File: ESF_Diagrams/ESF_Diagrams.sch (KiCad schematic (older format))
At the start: 37 parts, among them M1 Motor, M2 Motor, U2 AIR, U3 AIR

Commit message: Fix 2
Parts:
- added BT? (x48): Battery_Cell, symbol Battery_Cell
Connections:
- wire segments 88 -> 123
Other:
- moved on the sheet: BT?

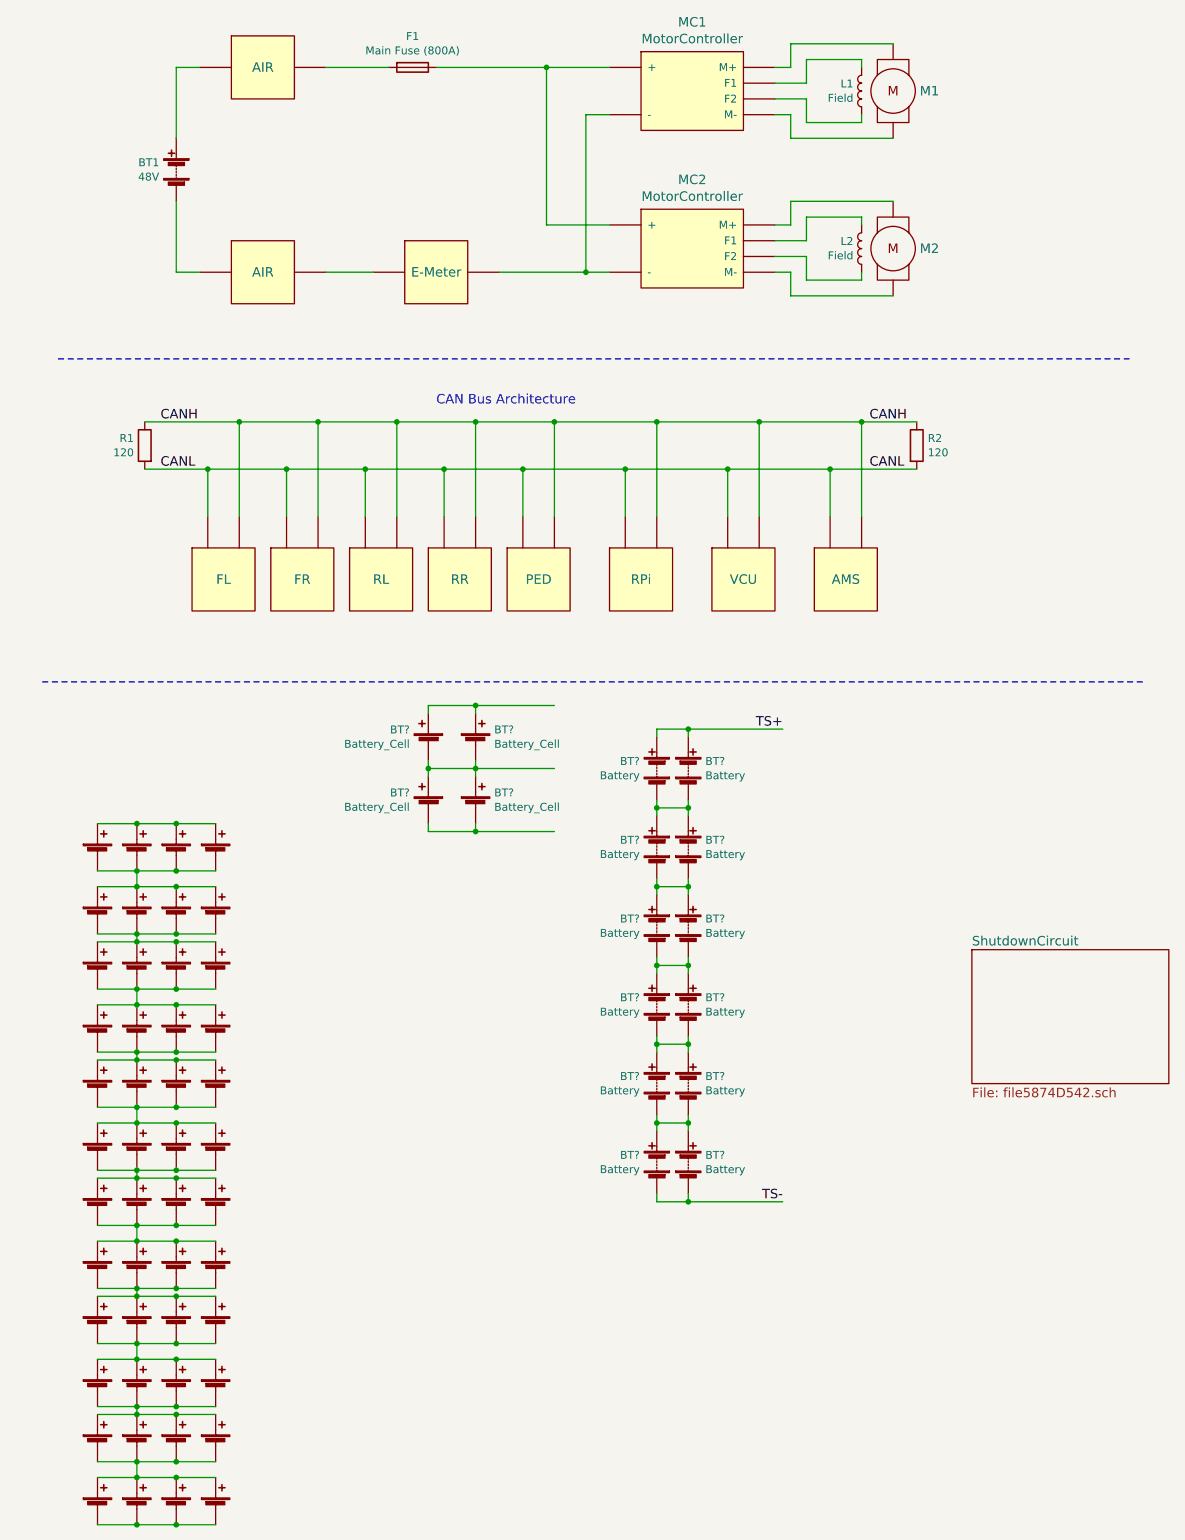
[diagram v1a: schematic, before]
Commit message: Remake battery drawing
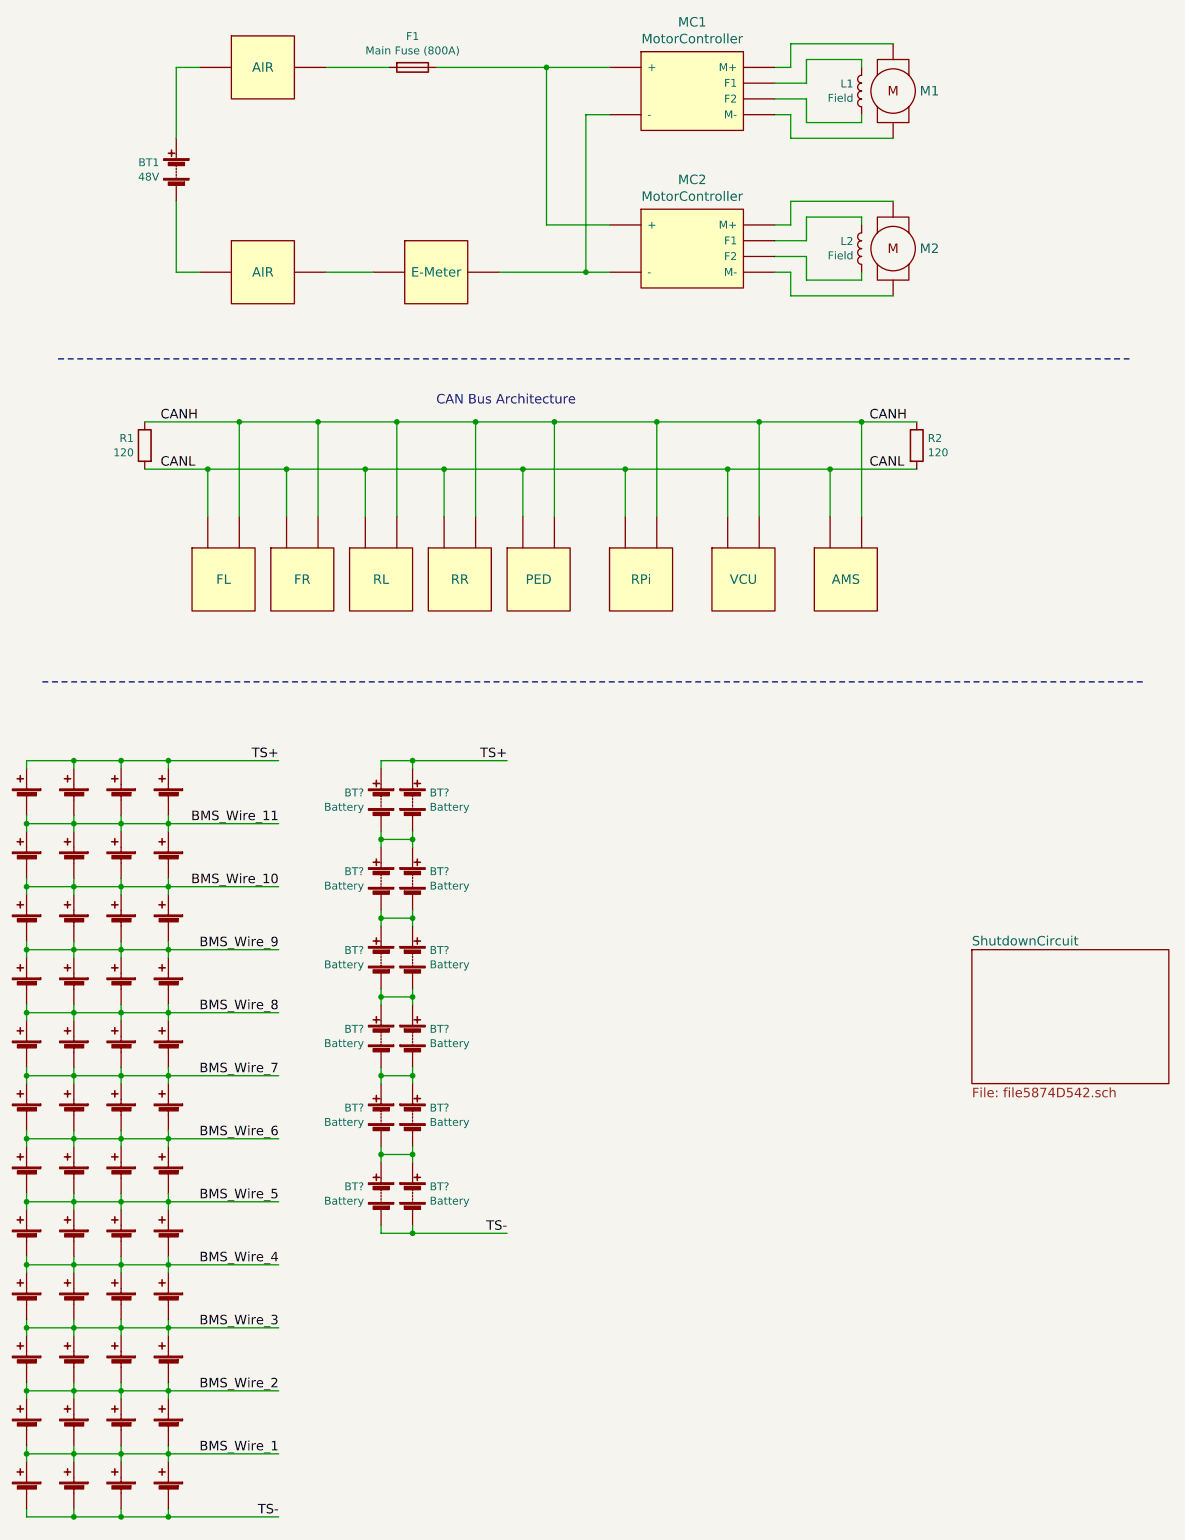
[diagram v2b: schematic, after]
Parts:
- removed BT? (x51): Battery_Cell, symbol Battery_Cell
- added BT? (x47): Battery_Cell, symbol Battery_Cell
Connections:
- net TS+: now also BT?.1 (+), BT?.1 (+), BT?.1 (+), BT?.1 (+)
- net TS-: now also BT?.2 (-), BT?.2 (-), BT?.2 (-), BT?.2 (-)
- net at MC1.~ (M-): now also L1.2; no longer M1.~
- net at MC2.~ (M-): now also L2.2; no longer M2.~
- net BMS_Wire_2: now reaches BT?.1 (+)
- net BMS_Wire_2: now also BT?.1 (+), BT?.1 (+), BT?.1 (+), BT?.2 (-), BT?.2 (-), BT?.2 (-), BT?.2 (-)
- net BMS_Wire_1: now reaches BT?.2 (-)
- net BMS_Wire_1: now also BT?.1 (+), BT?.1 (+), BT?.1 (+), BT?.1 (+), BT?.2 (-), BT?.2 (-), BT?.2 (-)
- new net: F1.1, MC1.~ (M-), MC2.~ (M-)
- new net: MC1.~ (M-), MC2.~ (M-), U?.~
- new net: M1.~, MC1.~ (M-)
- new net: M2.~, MC2.~ (M-)
- new net BMS_Wire_10: BT?.1 (+), BT?.1 (+), BT?.1 (+), BT?.1 (+), BT?.2 (-), BT?.2 (-), BT?.2 (-), BT?.2 (-)
- new net BMS_Wire_11: BT?.1 (+), BT?.1 (+), BT?.1 (+), BT?.1 (+), BT?.2 (-), BT?.2 (-), BT?.2 (-), BT?.2 (-)
- new net BMS_Wire_3: BT?.1 (+), BT?.1 (+), BT?.1 (+), BT?.1 (+), BT?.2 (-), BT?.2 (-), BT?.2 (-), BT?.2 (-)
- new net BMS_Wire_4: BT?.1 (+), BT?.1 (+), BT?.1 (+), BT?.1 (+), BT?.2 (-), BT?.2 (-), BT?.2 (-), BT?.2 (-)
- new net BMS_Wire_5: BT?.1 (+), BT?.1 (+), BT?.1 (+), BT?.1 (+), BT?.2 (-), BT?.2 (-), BT?.2 (-), BT?.2 (-)
- new net BMS_Wire_6: BT?.1 (+), BT?.1 (+), BT?.1 (+), BT?.1 (+), BT?.2 (-), BT?.2 (-), BT?.2 (-), BT?.2 (-)
- new net BMS_Wire_7: BT?.1 (+), BT?.1 (+), BT?.1 (+), BT?.1 (+), BT?.2 (-), BT?.2 (-), BT?.2 (-), BT?.2 (-)
- new net BMS_Wire_8: BT?.1 (+), BT?.1 (+), BT?.1 (+), BT?.1 (+), BT?.2 (-), BT?.2 (-), BT?.2 (-), BT?.2 (-)
- new net BMS_Wire_9: BT?.1 (+), BT?.1 (+), BT?.1 (+), BT?.1 (+), BT?.2 (-), BT?.2 (-), BT?.2 (-), BT?.2 (-)
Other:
- moved on the sheet: BT?

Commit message: Remade battery drawing to new configuration
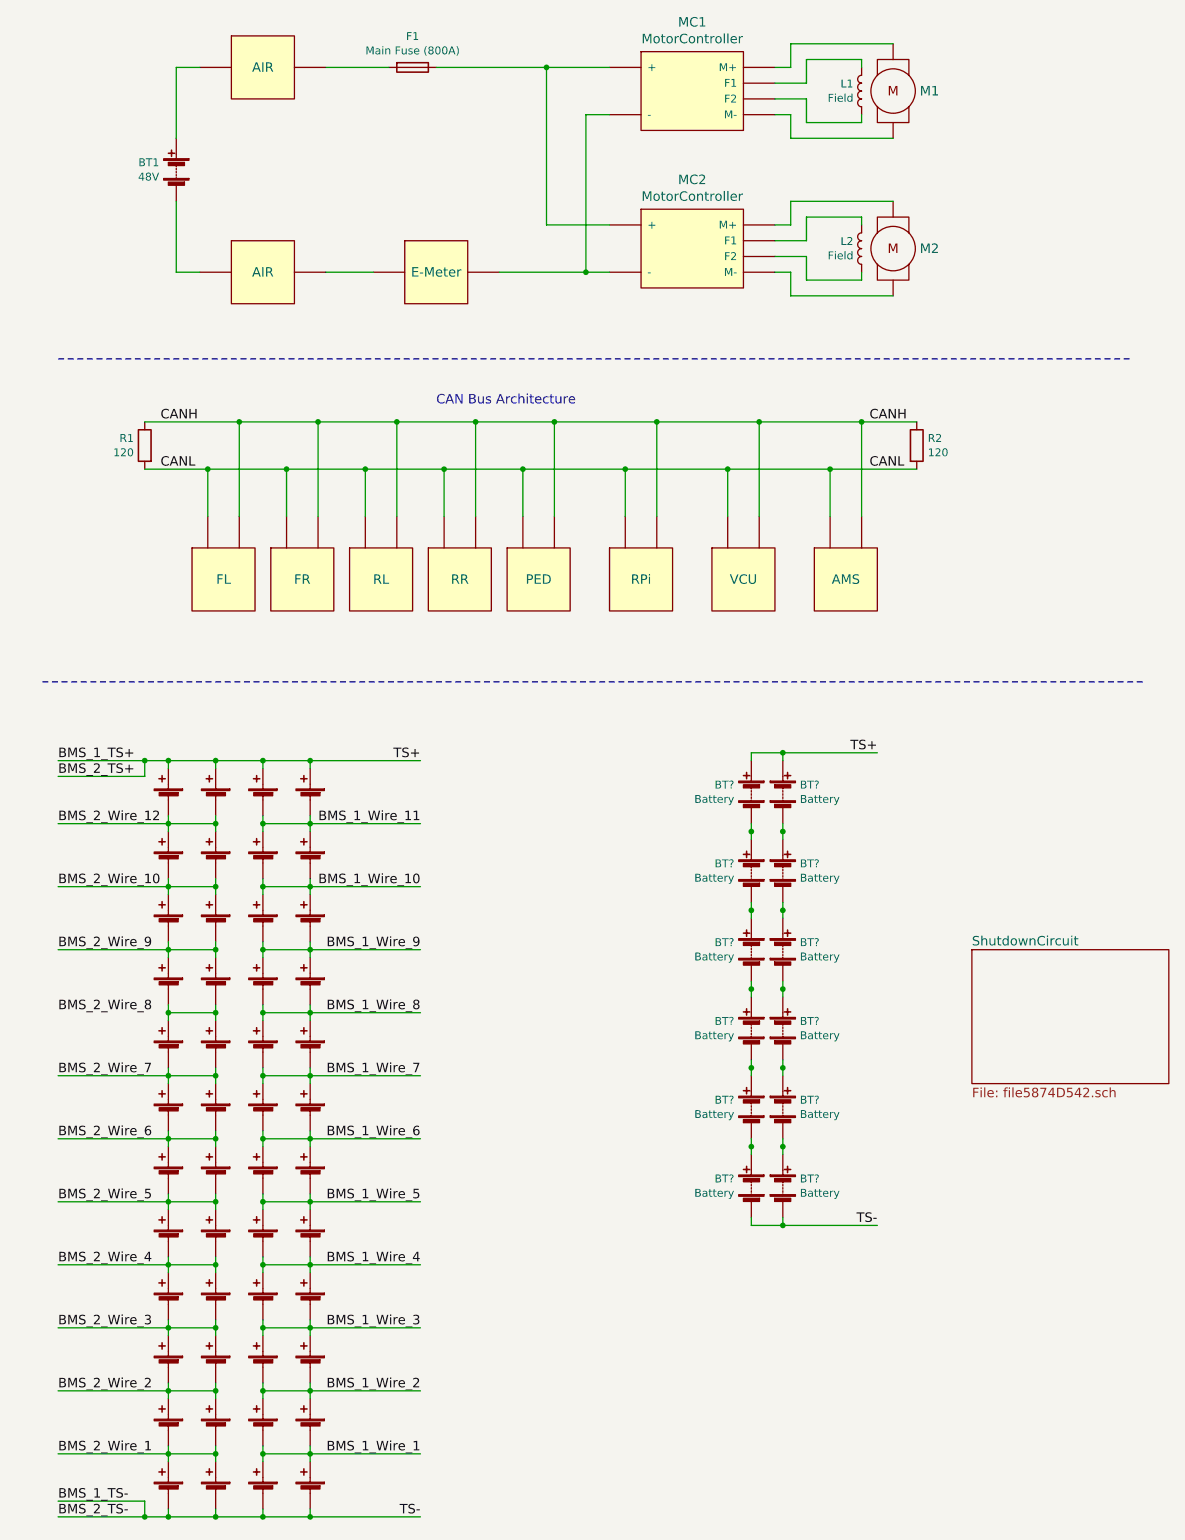
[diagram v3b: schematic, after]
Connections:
- net at MC1.~ (M-): now also L1.2; no longer M1.~
- net at MC2.~ (M-): now also L2.2; no longer M2.~
- net at BT?.1 (+), BT?.2 (-): no longer BT?.1 (+), BT?.2 (-) (x5)
- net BMS_Wire_1 renamed BMS_1_Wire_1
- net BMS_1_Wire_1: no longer BT?.1 (+), BT?.1 (+), BT?.2 (-), BT?.2 (-)
- net BMS_Wire_10 renamed BMS_1_Wire_10
- net BMS_1_Wire_10: no longer BT?.1 (+), BT?.1 (+), BT?.2 (-), BT?.2 (-)
- net BMS_Wire_11 renamed BMS_1_Wire_11
- net BMS_1_Wire_11: no longer BT?.1 (+), BT?.1 (+), BT?.2 (-), BT?.2 (-)
- net BMS_Wire_2 renamed BMS_1_Wire_2
- net BMS_1_Wire_2: no longer BT?.1 (+), BT?.1 (+), BT?.2 (-), BT?.2 (-)
- net BMS_Wire_3 renamed BMS_1_Wire_3
- net BMS_1_Wire_3: no longer BT?.1 (+), BT?.1 (+), BT?.2 (-), BT?.2 (-)
- net BMS_Wire_4 renamed BMS_1_Wire_4
- net BMS_1_Wire_4: no longer BT?.1 (+), BT?.1 (+), BT?.2 (-), BT?.2 (-)
- net BMS_Wire_5 renamed BMS_1_Wire_5
- net BMS_1_Wire_5: no longer BT?.1 (+), BT?.1 (+), BT?.2 (-), BT?.2 (-)
- net BMS_Wire_6 renamed BMS_1_Wire_6
- net BMS_1_Wire_6: no longer BT?.1 (+), BT?.1 (+), BT?.2 (-), BT?.2 (-)
- net BMS_Wire_7 renamed BMS_1_Wire_7
- net BMS_1_Wire_7: no longer BT?.1 (+), BT?.1 (+), BT?.2 (-), BT?.2 (-)
- net BMS_Wire_8: no longer names the net of BT?.1 (+), BT?.1 (+), BT?.2 (-), BT?.2 (-)
- net BMS_Wire_8: no longer BT?.1 (+), BT?.1 (+), BT?.2 (-), BT?.2 (-)
- net BMS_Wire_9 renamed BMS_1_Wire_9
- net BMS_1_Wire_9: no longer BT?.1 (+), BT?.1 (+), BT?.2 (-), BT?.2 (-)
- net TS+ renamed BMS_1_TS+
- net TS- renamed BMS_1_TS-
- new net: F1.1, MC1.~ (M-), MC2.~ (M-)
- new net: MC1.~ (M-), MC2.~ (M-), U?.~
- new net: M1.~, MC1.~ (M-)
- new net: M2.~, MC2.~ (M-)
- new net: BT?.1 (+), BT?.2 (-) (x5)
- new net BMS_1_Wire_8: BT?.1 (+), BT?.1 (+), BT?.2 (-), BT?.2 (-)
- new net BMS_2_Wire_1: BT?.1 (+), BT?.1 (+), BT?.2 (-), BT?.2 (-)
- new net BMS_2_Wire_10: BT?.1 (+), BT?.1 (+), BT?.2 (-), BT?.2 (-)
- new net BMS_2_Wire_12: BT?.1 (+), BT?.1 (+), BT?.2 (-), BT?.2 (-)
- new net BMS_2_Wire_2: BT?.1 (+), BT?.1 (+), BT?.2 (-), BT?.2 (-)
- new net BMS_2_Wire_3: BT?.1 (+), BT?.1 (+), BT?.2 (-), BT?.2 (-)
- new net BMS_2_Wire_4: BT?.1 (+), BT?.1 (+), BT?.2 (-), BT?.2 (-)
- new net BMS_2_Wire_5: BT?.1 (+), BT?.1 (+), BT?.2 (-), BT?.2 (-)
- new net BMS_2_Wire_6: BT?.1 (+), BT?.1 (+), BT?.2 (-), BT?.2 (-)
- new net BMS_2_Wire_7: BT?.1 (+), BT?.1 (+), BT?.2 (-), BT?.2 (-)
- new net BMS_2_Wire_9: BT?.1 (+), BT?.1 (+), BT?.2 (-), BT?.2 (-)
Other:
- moved on the sheet: BT?

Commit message: Accumulator changes
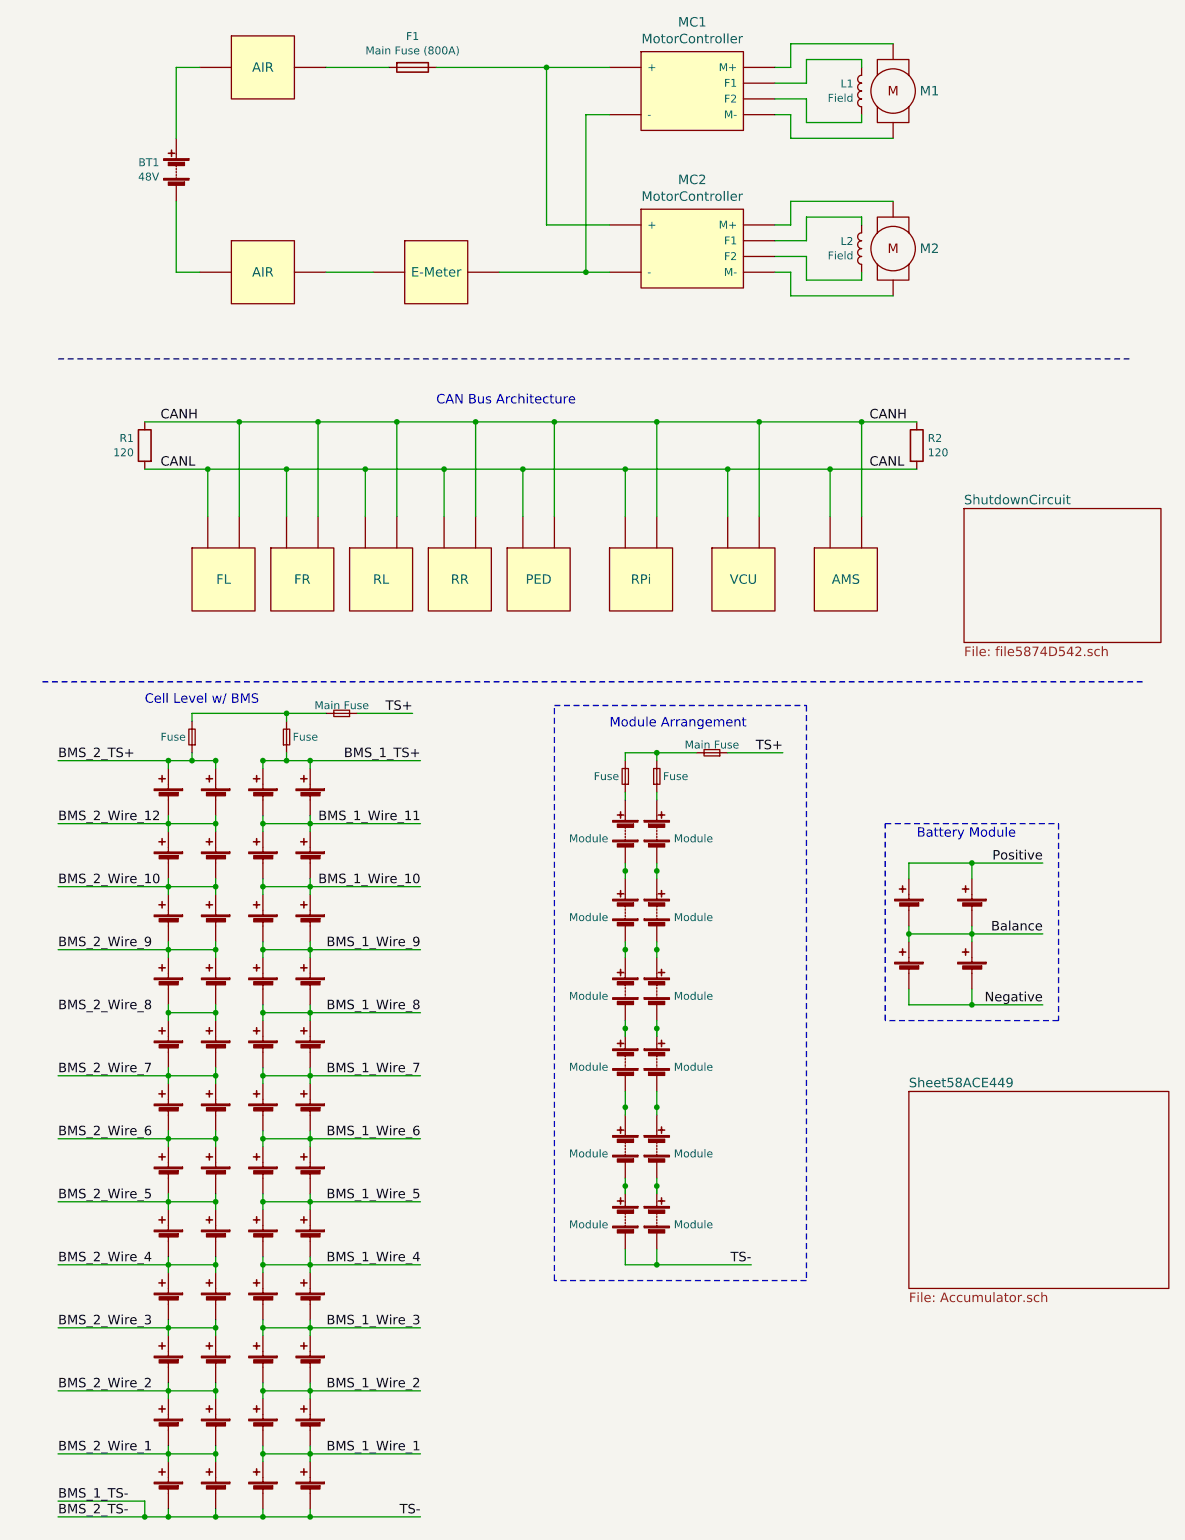
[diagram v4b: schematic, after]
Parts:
- removed BT? (x11): Battery, symbol Battery
- added BT? (x4): Battery_Cell, symbol Battery_Cell
- added BT? (x11): Module, symbol Battery
- added F? (x4): Fuse, symbol Fuse_Small
- added F? (x2): Main Fuse, symbol Fuse_Small
- BT?: value Battery -> Module
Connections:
- net BMS_1_TS+: now also F?.1; no longer BT?.1 (+), BT?.1 (+), BT?.1 (+)
- net BMS_1_TS-: now also BT?.2 (-), BT?.2 (-)
- net at MC1.~ (M-): now also L1.2; no longer M1.~
- net at MC2.~ (M-): now also L2.2; no longer M2.~
- net at BT?.2 (-): now also BT?.1 (+)
- new net: F1.1, MC1.~ (M-), MC2.~ (M-)
- new net: MC1.~ (M-), MC2.~ (M-), U?.~
- new net: M1.~, MC1.~ (M-)
- new net: M2.~, MC2.~ (M-)
- new net: BT?.1 (+), F?.1 (x2)
- new net: BT?.1 (+), BT?.2 (-) (x9)
- new net: F?.2, F?.2, F?.2 (x2)
- new net BMS_2_TS+: BT?.1 (+), BT?.1 (+), F?.1
- new net Balance: BT?.1 (+), BT?.1 (+), BT?.2 (-), BT?.2 (-)
- new net Negative: BT?.2 (-), BT?.2 (-)
- new net Positive: BT?.1 (+), BT?.1 (+)
- new net TS+: F?.1, F?.1
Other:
- note added: "Battery Module"
- note added: "Cell Level w/ BMS"
- note added: "Module Arrangement"
